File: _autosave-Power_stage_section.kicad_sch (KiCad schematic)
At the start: 31 parts, among them IC1 LM66200DRLR, Q1 BSC082N10LSG, Q2 BSC082N10LSG, U2 IRS2186, U3 TLV70012_SOT23-5

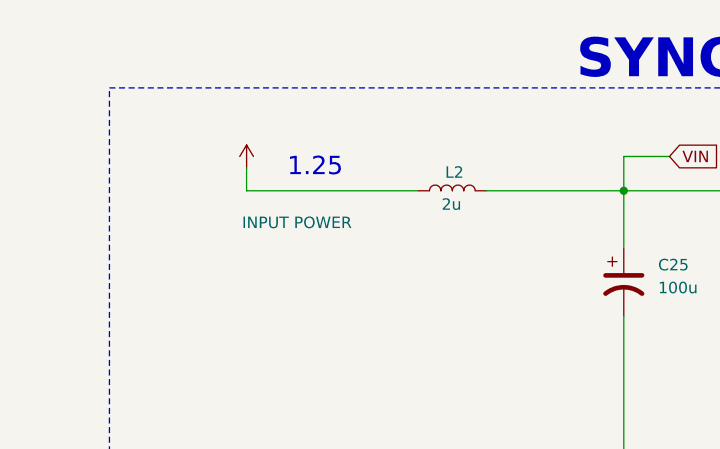
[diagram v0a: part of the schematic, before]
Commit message: Placement finished routing started
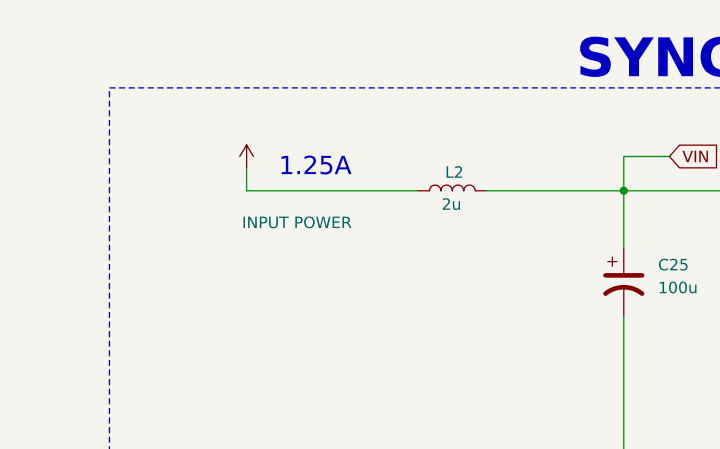
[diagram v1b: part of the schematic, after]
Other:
- note added: "1.25A"
- note removed: "1.25"
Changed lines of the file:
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@@
 		)
 	)
-	(text "1.25\n"
+	(text "1.25A\n"
 		(exclude_from_sim no)
 		(at 45.72 27.94 0)
